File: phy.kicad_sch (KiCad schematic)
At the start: 56 parts, among them Q1 BSS138LT1G, Q2 BSS138LT1G, Q3 BSS138LT1G, U2 DP83867IRPAPR

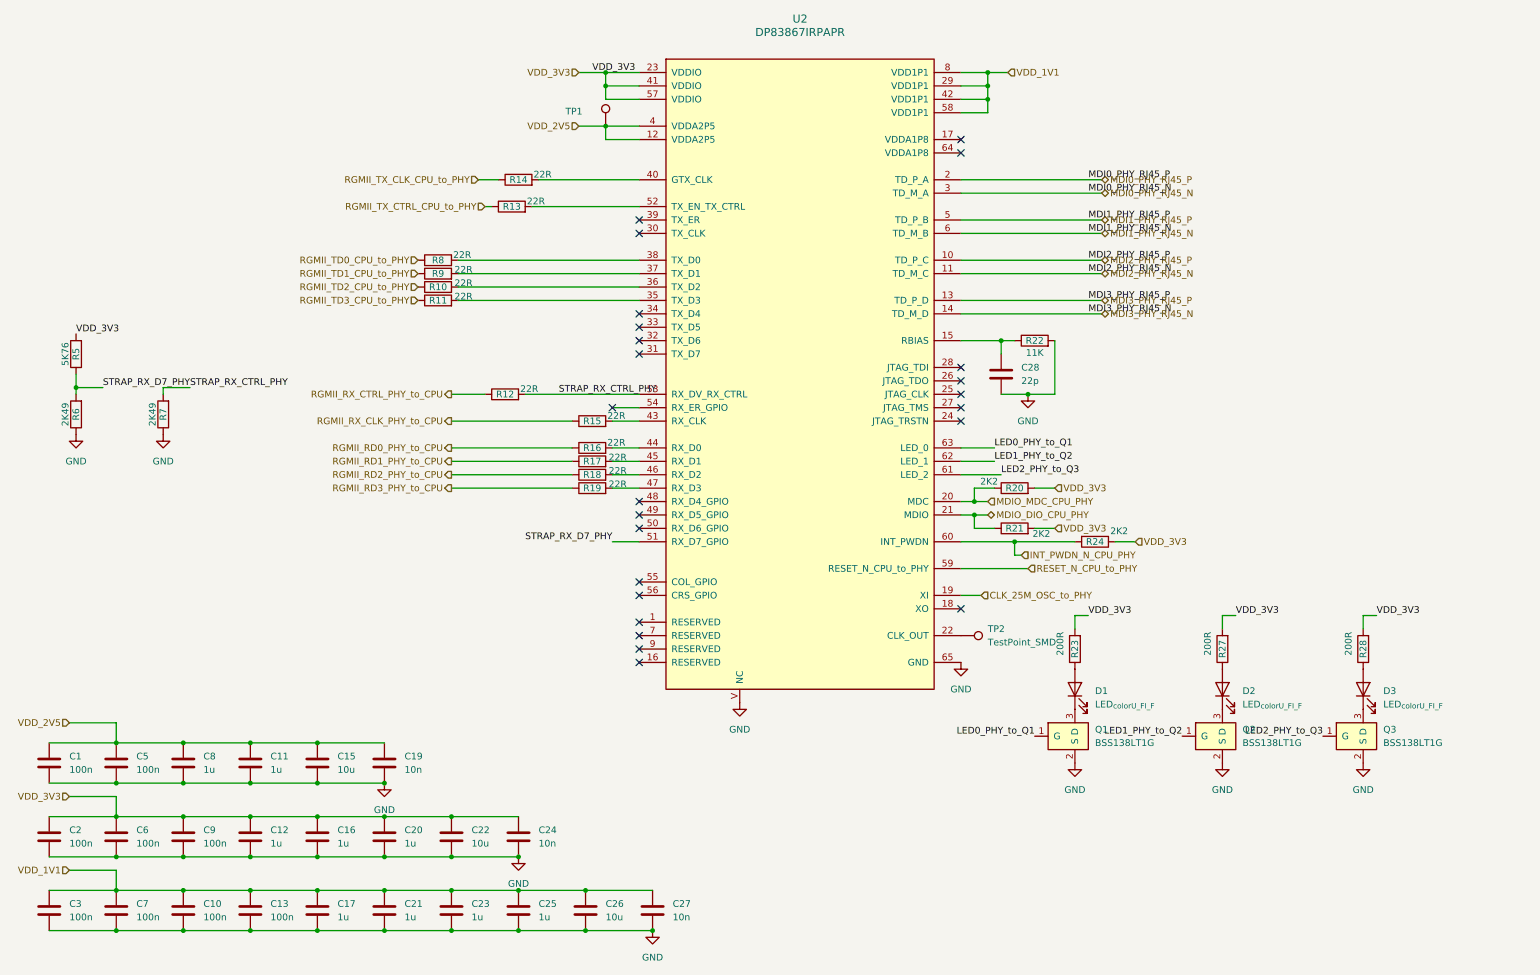
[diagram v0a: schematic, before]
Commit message: Improve schematic readability across all sheets
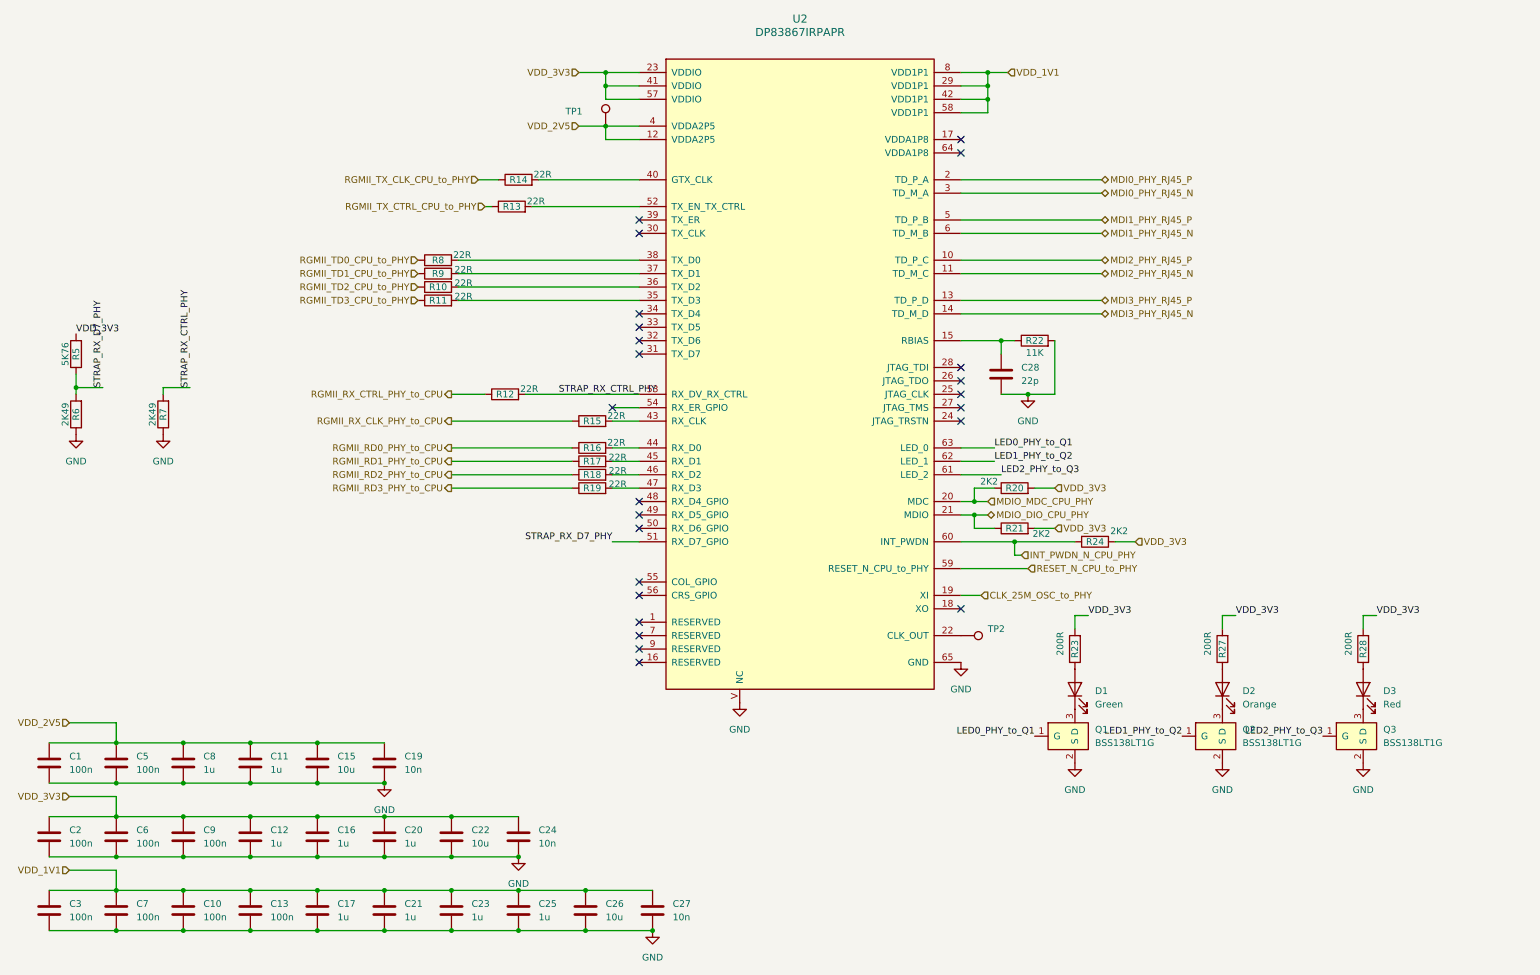
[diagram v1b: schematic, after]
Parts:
- D1: value LED_{color}_{U_F}_{I_F} -> Green
- D2: value LED_{color}_{U_F}_{I_F} -> Orange
- D3: value LED_{color}_{U_F}_{I_F} -> Red
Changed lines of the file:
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@@
 		)
 	)
-	(label "MDI2_PHY_RJ45_P"
-		(at 218.44 58.42 0)
-		(effects
-			(font
-				(size 1.27 1.27)
-			)
-			(justify left bottom)
-		)
-	)
-	(label "MDI2_PHY_RJ45_N"
-		(at 218.44 60.96 0)
-		(effects
-			(font
-				(size 1.27 1.27)
-			)
-			(justify left bottom)
-		)
-	)
 	(label "LED2_PHY_to_Q3"
 		(at 262.89 148.59 180)
@@
 		)
 	)
-	(label "MDI0_PHY_RJ45_P"
-		(at 218.44 43.18 0)
-		(effects
-			(font
-				(size 1.27 1.27)
-			)
-			(justify left bottom)
-		)
-	)
 	(label "LED1_PHY_to_Q2"
 		(at 236.22 148.59 180)
@@
 		)
 	)
-	(label "MDI0_PHY_RJ45_N"
-		(at 218.44 45.72 0)
-		(effects
-			(font
-				(size 1.27 1.27)
-			)
-			(justify left bottom)
-		)
-	)
 	(label "VDD_3V3"
 		(at 273.05 125.73 0)
@@
 	)
 	(label "STRAP_RX_CTRL_PHY"
-		(at 48.26 82.55 0)
+		(at 48.26 82.55 90)
 		(effects
 			(font
@@
 	)
 	(label "STRAP_RX_D7_PHY"
-		(at 31.75 82.55 0)
-		(effects
-			(font
-				(size 1.27 1.27)
-			)
-			(justify left bottom)
-		)
-	)
-	(label "MDI3_PHY_RJ45_N"
-		(at 218.44 68.58 0)
+		(at 31.75 82.55 90)
 		(effects
 			(font
@@
 		)
 	)
-	(label "MDI3_PHY_RJ45_P"
-		(at 218.44 66.04 0)
-		(effects
-			(font
-				(size 1.27 1.27)
-			)
-			(justify left bottom)
-		)
-	)
-	(label "VDD_3V3"
-		(at 124.46 22.86 0)
-		(effects
-			(font
-				(size 1.27 1.27)
-			)
-			(justify left bottom)
-		)
-	)
-	(label "MDI1_PHY_RJ45_N"
-		(at 218.44 53.34 0)
-		(effects
-			(font
-				(size 1.27 1.27)
-			)
-			(justify left bottom)
-		)
-	)
-	(label "MDI1_PHY_RJ45_P"
-		(at 218.44 50.8 0)
-		(effects
-			(font
-				(size 1.27 1.27)
-			)
-			(justify left bottom)
-		)
-	)
 	(label "STRAP_RX_D7_PHY"
 		(at 128.27 111.76 180)
@@
 		(property "Value" "TestPoint_SMD"
 			(at 199.39 130.8099 90)
+			(hide yes)
 			(effects
 				(font
@@
 			)
 		)
-		(property "Value" "LED_{color}_{U_F}_{I_F}"
+		(property "Value" "Red"
 			(at 274.32 142.5574 90)
 			(effects
@@
 			)
 		)
-		(property "Value" "LED_{color}_{U_F}_{I_F}"
+		(property "Value" "Green"
 			(at 219.71 142.5574 90)
 			(effects
@@
 			)
 		)
-		(property "Value" "LED_{color}_{U_F}_{I_F}"
+		(property "Value" "Orange"
 			(at 247.65 142.5574 90)
 			(effects

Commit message: Connect LED1 and LED2 nets to Q2 Q3 gates
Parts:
- C11, C12, C16, C17, C20, C21, C23, C25, C8: Digikey TBD -> 490-10694-1-ND; LCSC TBD -> C77006
- C15, C22, C26: Digikey TBD -> 490-13811-2-ND; LCSC TBD -> C76991
- C19, C24, C27: Digikey TBD -> 490-4516-1-ND; LCSC TBD -> C77019
- C28: Digikey TBD -> 490-5868-1-ND; LCSC TBD -> C76960
- D1: Digikey TBD -> 160-1179-1-ND; LCSC LTST-C190GKT -> C125090
- D2: Digikey TBD -> 160-1413-1-ND; LCSC C7297440 -> C284931
- D3: Digikey TBD -> 160-1415-1-ND; LCSC C913101 -> C94868
- Q1, Q2, Q3: Digikey TBD -> BSS138LT1GOSCT-ND; LCSC TBD -> C82045
- R10, R11, R12, R13, R14, R15, R16, R17, R18, R19, R8, R9: Digikey TBD -> 541-3973-1-ND; LCSC TBD -> C2076943
- R20, R21, R24: Digikey TBD -> 541-3971-1-ND; LCSC TBD -> C2076947
- R22: Digikey TBD -> 541-4691-1-ND; LCSC TBD -> C1730800
- R23, R27, R28: Digikey TBD -> 541-3995-1-ND; LCSC TBD -> C843896
- R5: Digikey TBD -> 541-5031-1-ND; LCSC TBD -> C4180495
- R6, R7: Digikey TBD -> 541-4867-1-ND; LCSC TBD -> C1730862
- U2: Digikey TBD -> 296-46083-1-ND; LCSC TBD -> C477933
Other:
- title: (none) -> PHY
- moved on the sheet: R7

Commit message: Fix RX_CTRL and RX_D7 straps, oscillator load, RBIAS
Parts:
- removed C28: 22p, KL_Footprints:C_0402, symbol KL_C:C_22p_50V_5pct_C0G_0402
- removed R6: 2K49, KL_Footprints:R_0402, symbol KL_R:R_2K49_0.063W_1pct_0402
- added R30: 5K76, KL_Footprints:R_0402, symbol KL_R:R_5K76_0.063W_1pct_0402
- R5: value 5K76 -> 2K49; symbol KL_R:R_5K76_0.063W_1pct_0402 -> KL_R:R_2K49_0.063W_1pct_0402; Digikey 541-5031-1-ND -> 541-4867-1-ND; LCSC C4180495 -> C1730862; MPN CRCW04025K76FKEDC -> CRCW04022K49FKEDC; Mouser 71-CRCW04025K76FKEDC -> 71-CRCW04022K49FKEDC
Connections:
- net STRAP_RX_CTRL_PHY: now also R30.1
- net VDD_3V3: now also R30.2

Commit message: Add 1uF decoupling on PHY pins 4, 12, 41, 42
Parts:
- added C37, C38, C39, C40: 1u, KL_Footprints:C_0402, symbol KL_C:C_1u_16V_10pct_X5R_0402
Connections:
- net GND: now also C37.2, C38.2, C39.2, C40.2
- net VDD_1V1: now also C38.1
- net VDD_2V5: now also C39.1, C40.1
- net VDD_3V3: now also C37.1

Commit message: Mirror J1 MDI pins, add LED_0 mirror-mode strap
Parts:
- added R31: 5K76, KL_Footprints:R_0402, symbol KL_R:R_5K76_0.063W_1pct_0402
- added R32: 2K49, KL_Footprints:R_0402, symbol KL_R:R_2K49_0.063W_1pct_0402
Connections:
- net GND: now also R32.2
- net LED0_PHY_to_Q1: now also R31.1, R32.1
- net VDD_3V3: now also R31.2

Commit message: Switch BOM to in-stock LCSC parts, U3 to TLV73311
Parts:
- C1, C10, C13, C2, C3, C5, C6, C7, C9: Digikey 445-6901-1-ND -> (none); LCSC C2181802 -> C307331; MPN CGA2B3X7R1V104K050BB -> CL05B104KB54PNC; Mouser 810-CGA2B3X7R1V104K -> (none); Voltage_in_V 35 -> 50
- R10, R11, R12, R13, R14, R15, R16, R17, R18, R19, R8, R9: Digikey 541-3973-1-ND -> (none); LCSC C2076943 -> C25092; MPN CRCW040222R0FKEDC -> 0402WGF220JTCE; Mouser 71-CRCW040222R0FKEDC -> (none)
- R22: Digikey 541-4691-1-ND -> (none); LCSC C1730800 -> C2909313; MPN CRCW040211K0FKEDC -> FRC0402F1102TS; Mouser 71-CRCW040211K0FKEDC -> (none)
- R23, R27, R28: Digikey 541-3995-1-ND -> (none); LCSC C843896 -> C25087; MPN CRCW0402200RFKEDC -> 0402WGF2000TCE; Mouser 71-CRCW0402200RFKEDC -> (none)
- R30, R31: Digikey 541-5031-1-ND -> (none); LCSC C4180495 -> C5153969; MPN CRCW04025K76FKEDC -> FRC0402F5761TS; Mouser 71-CRCW04025K76FKEDC -> (none)
